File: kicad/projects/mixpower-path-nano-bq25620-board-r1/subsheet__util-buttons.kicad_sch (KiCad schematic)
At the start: 17 parts, among them SW1 TS-A002, SW2 TS-A002, SW3 TS-1088, U11 RT9829GQW, U12 RT9829GQW

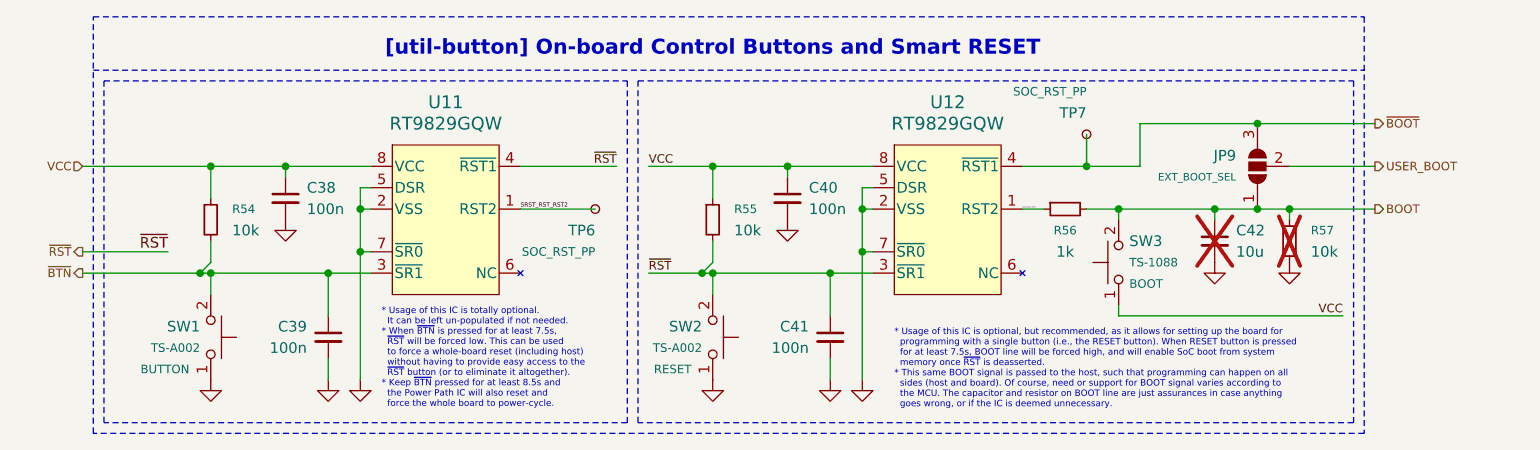
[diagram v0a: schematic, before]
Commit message: fix: put all subsheets in root of the Kicad project, regenerate schematics plots
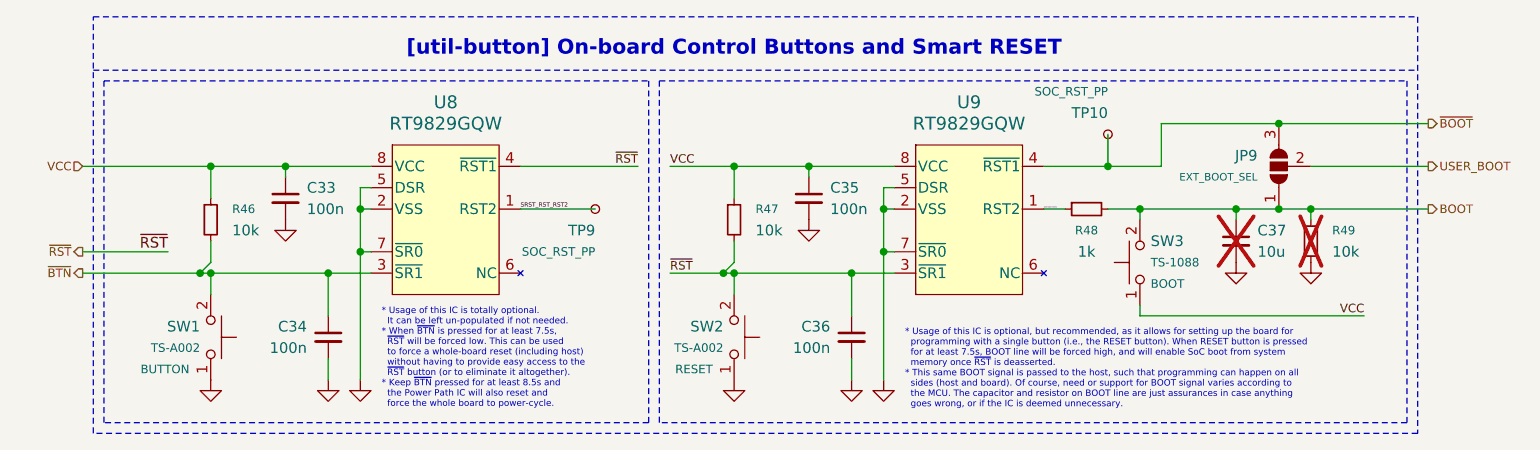
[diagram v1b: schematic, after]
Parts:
- renumbered C38 to C33, C39 to C34, C40 to C35, C41 to C36, C42 to C37, R54 to R46, R55 to R47, R56 to R48, R57 to R49, TP7 to TP10, TP6 to TP9, U11 to U8, U12 to U9
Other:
- title: (none) -> mixpower-path-nano-bq25620-board
- moved on the sheet: C35, C36, C37, JP9, R47, R48, R49, SW2, SW3, TP10, U9
